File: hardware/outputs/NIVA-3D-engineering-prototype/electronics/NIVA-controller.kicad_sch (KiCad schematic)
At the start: 49 parts, among them J1 INSERT TAIL (JST GH 10, keyed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, J2 CARTRIDGE SPRING CONTACTS (pa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, J3 SERVICE PADS (TC2030-NL, unde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, SW1 KMR221G (C&K KMR2), U1 ESP32-C3-MINI-1-N4, U2 MCP3208-CI/SL, U3 LSM6DSO32TR, U5 TLV75533PDBVR, U6 MAX17048G+T10

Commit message: NIVA Rev C: KiCad placement prototype PCB and audited enclosure
PCB: 4-layer 34x48 mm board generated from the netlist with pcbnew,
official Espressif module footprint + STEP, KiCad library models,
antenna keepout, In1 GND plane, corner notches around the enclosure
bosses. Freerouting stalled at ~40 unrouted connections, so the board
is delivered and labelled as an UNROUTED PLACEMENT PROTOTYPE.

Enclosure: new niva_layout.py shared by PCB and FreeCAD generators;
continuous gasket with boss hard stops, bossed cover screws, PCB bosses,
ledges and clamp ribs, connector-height keyed tail aperture, light pipe
to emitters, bay ceiling, spring-contact cartridge lid, cradle rails,
latch and L/R keys. Full pairwise audit against the KiCad PCBA STEP.

Co-Authored-By: Claude Opus 5.5 <noreply@anthropic.com>
Claude-Session: https://claude.ai/code/session_01HNzeJFE5uNHjapog53SHnm
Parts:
- added H1, H2: M2 board screw, MountingHole:MountingHole_2.2mm_M2, symbol Mechanical:MountingHole
- J3: now left out of the parts list

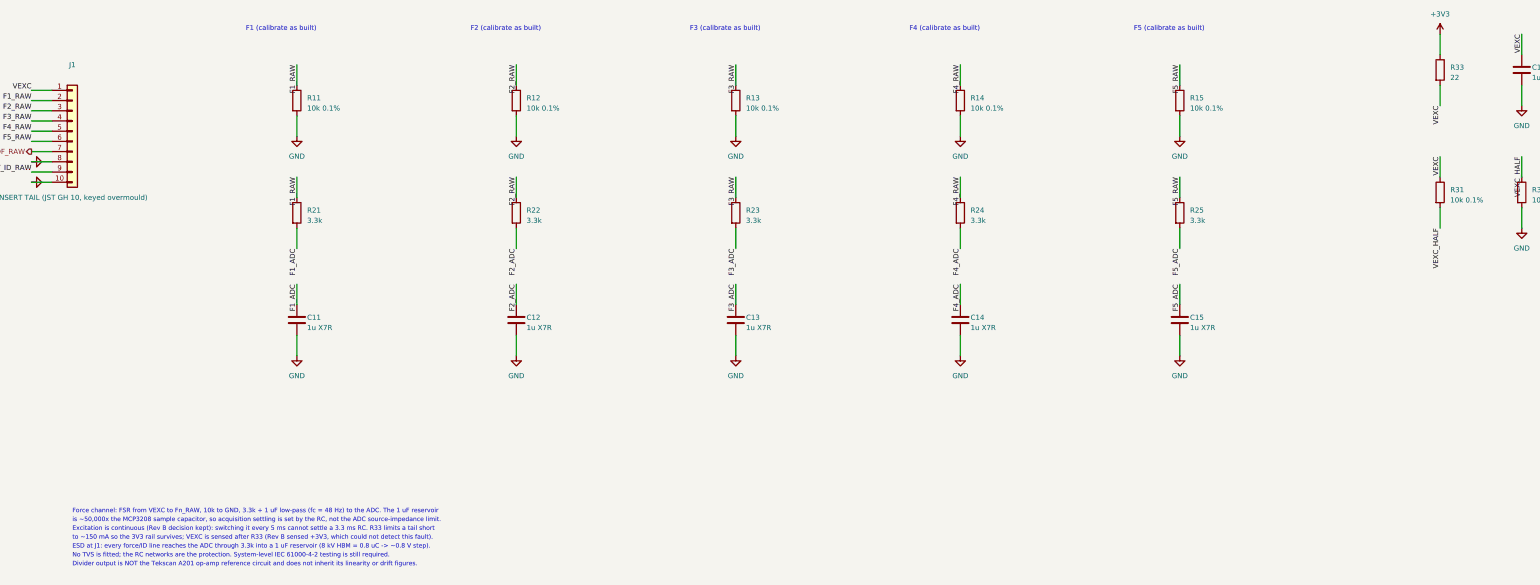
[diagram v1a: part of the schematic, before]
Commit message: NIVA Rev C: documentation, final exports, captioned PCB renders
- ELECTRICAL-REVIEW.md, PRINT-AND-ASSEMBLY.md and package README
- R33 raised to 220R (22R would dissipate 0.5 W in an 0603 on a tail short)
- deterministic schematic UUIDs; generators accept only KiCad 9 libraries
- regenerated ERC/netlist/BOM/PCB/DRC/PCBA STEP+GLB/assembly PDFs
- Blender scene builder and caption tool; KiCad raytraced PCB views
- stale Rev B generated outputs removed (kept in git history)

Co-Authored-By: Claude Opus 5.5 <noreply@anthropic.com>
Claude-Session: https://claude.ai/code/session_01HNzeJFE5uNHjapog53SHnm
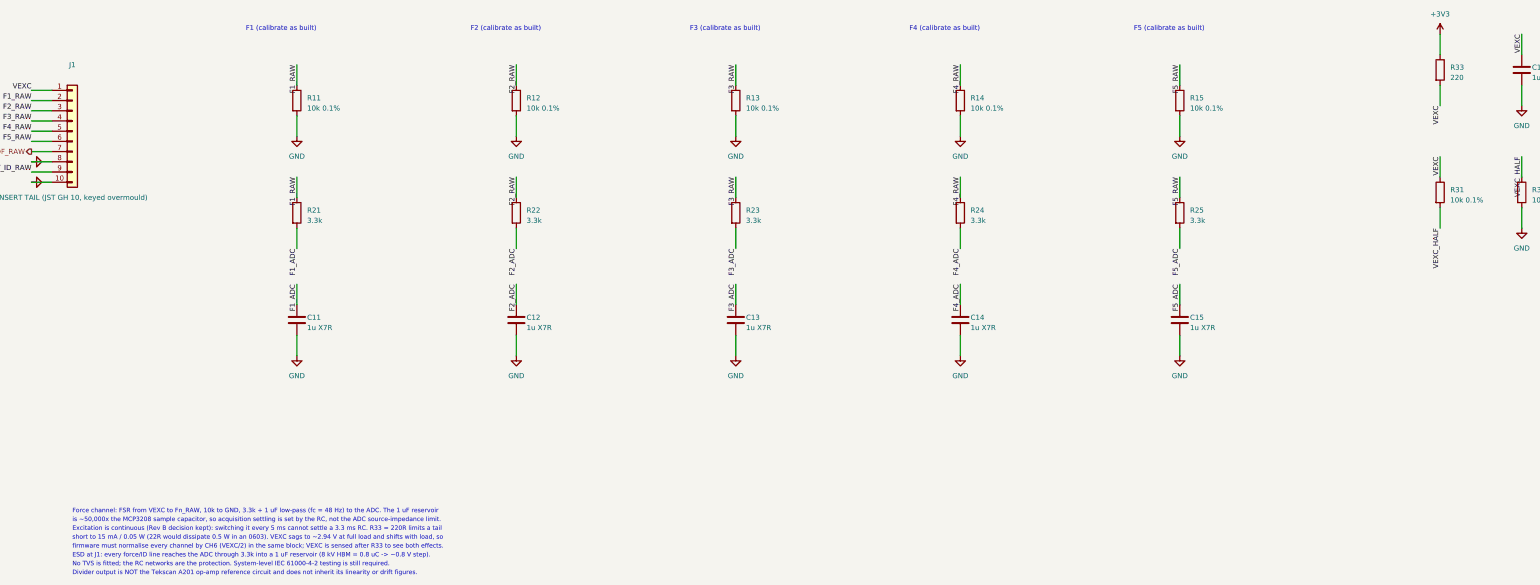
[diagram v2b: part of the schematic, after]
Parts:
- R33: value 22 -> 220
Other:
- note added: "Excitation is continuous (Rev B decision kept): switching it every 5 ms cannot settle a 3.3 ms RC. R33 = 220R limits a tail"
- note added: "firmware must normalise every channel by CH6 (VEXC/2) in the same block; VEXC is sensed after R33 to see both effects."
- note added: "short to 15 mA / 0.05 W (22R would dissipate 0.5 W in an 0603). VEXC sags to ~2.94 V at full load and shifts with load, so"
- note removed: "Excitation is continuous (Rev B decision kept): switching it every 5 ms cannot settle a 3.3 ms RC. R33 limits a tail short"
- note removed: "to ~150 mA so the 3V3 rail survives; VEXC is sensed after R33 (Rev B sensed +3V3, which could not detect this fault)."

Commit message: Add cartridge interconnect PCB, charging dock PCB and dock enclosure; ratiometric ADC reference
- Pod schematic: MCP3208 VREF driven from VEXC (the sensor excitation rail) so every
  channel is ratiometric in hardware; CH6 reads +3V3/2 as a rail monitor.
- Cartridge: 3.4 mm interconnect strip (cell leads, polyfuse, lid-plate leads, underside
  dock pads), hand-routed; ERC/DRC clean with schematic parity.
- Dock: USB-C sink, MCP73831 charger gated by an LM393 NTC window comparator, spring
  pins to the cartridge pads; autorouted (Freerouting) and DRC clean.
- Fabrication data for both boards written only as review-only sets with open blockers.
- Dock enclosure (base, top with keyed well, tab ledge, snap latch, light pipe) generated
  from niva_layout.py; interference audit reports only the expected spring-pin contacts.
- Shared CAD helpers and cartridge builders moved to niva_cad_lib.py.

Co-Authored-By: Claude Opus 5.5 <noreply@anthropic.com>
Claude-Session: https://claude.ai/code/session_01HNzeJFE5uNHjapog53SHnm
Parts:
- R31, R32: value 10k 0.1% -> 10k 1%
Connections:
- net +3V3: now also R31.1; no longer C19.1, R30.1, U2.15 (Vref)
- net VEXC: now also C19.1, R30.1, U2.15 (Vref); no longer R31.1
- net VEXC_HALF renamed V33_HALF
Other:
- note added: "C4 at VDD pin 16, C19 at VREF pin 15. VREF = VEXC (the excitation node itself), so force, ID and"
- note added: "VEXC: ~2048 nominal, rising as VEXC sags, full scale on a tail short (fault flag)."
- note added: "piezo readings are ratiometric in hardware: no firmware normalisation. CH6 reads +3V3/2 against"
- note added: "short to 15 mA / 0.05 W (22R would dissipate 0.5 W in an 0603). VEXC sags to ~2.94 V at full load and moves with load,"
- note added: "which cancels exactly because the ADC reference (pin 15) is the same VEXC node (MCP3208 IREF <= 150 uA -> <= 33 mV)."
- note removed: "C4 at VDD pin 16, C19 at VREF pin 15. VREF = +3V3, so force and ID readings are"
- note removed: "firmware must normalise every channel by CH6 (VEXC/2) in the same block; VEXC is sensed after R33 to see both effects."
- note removed: "ratiometric; CH6 (VEXC/2) is read every block to detect excitation faults."
- note removed: "short to 15 mA / 0.05 W (22R would dissipate 0.5 W in an 0603). VEXC sags to ~2.94 V at full load and shifts with load, so"
